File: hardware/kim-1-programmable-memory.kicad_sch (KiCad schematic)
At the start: 21 parts, among them J1 Conn_02x01, J3 EDGE_CONN, Q1 DMG2305UX, SW1 RESET, U1 74LVC541, U2 74LVC541, U3 74LVC245, U4 74LVC1G04, U6 74LVC1G38, U7 74LVC1G27, U8 PicoW

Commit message: New board design usign the RAMRW line
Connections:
- net RAMR~{W}: now reaches J3.Z (RAMRW)
- net RAMR~{W}: now also U4.2
- net R/~{W}: no longer names the net of J3.V (R/~{W})
- net R/~{W}: no longer U4.2
- net ~{R}/W: no longer names the net of J3.W (~{R}/W)
- net ~{R}/W: no longer U3.1 (A->B)
- net ~{R}/W' renamed RAM~{R}W
- net RAM~{R}W: now also U3.1 (A->B)
- no-connect marks 17 -> 18
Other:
- moved on the sheet: C1, C2, C3, C4, R2, SW1, U1, U2, U3, U4

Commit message: New board design
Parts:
- removed C4: 100nF, Capacitor_SMD:C_0603_1608Metric_Pad1.08x0.95mm_HandSolder, symbol Device:C_Small
- removed U4: 74LVC1G04, Package_TO_SOT_SMD:SOT-23-5_HandSoldering, symbol 74xGxx:74LVC1G04
- added C1, C11, C7: 100nF, Capacitor_SMD:C_0603_1608Metric_Pad1.08x0.95mm_HandSolder, symbol Device:C_Small
- added C10: 10uF, Capacitor_SMD:C_0603_1608Metric_Pad1.08x0.95mm_HandSolder, symbol Device:C_Small
- added D1: HDD, LED_SMD:LED_0603_1608Metric_Pad1.05x0.95mm_HandSolder, symbol Device:LED_Small
- added J3: VGA, Connector_Dsub:DSUB-15-HD_Female_Horizontal_P2.29x1.98mm_EdgePinOffset3.03mm_Housed_MountingHolesOffset4.94mm, symbol Connector:DA15_Receptacle_MountingHoles
- added J4: VIdeo Out, CUI_Devices:CUI_RCJ-014, symbol Connector:Conn_Coaxial_Small
- added J5: Micro_SD_Card_Det1, Micro-SD:SD_Card_Holder_SMD_WQ21801-B2180-7F, symbol Connector:Micro_SD_Card_Det1
- added R10, R11, R8, R9: 40R, Resistor_SMD:R_0603_1608Metric_Pad0.98x0.95mm_HandSolder, symbol Device:R_Small_US
- added R12: 470R, Resistor_SMD:R_0603_1608Metric_Pad0.98x0.95mm_HandSolder, symbol Device:R_Small_US
- added R13, R14, R15, R16: 270R, Resistor_SMD:R_0603_1608Metric_Pad0.98x0.95mm_HandSolder, symbol Device:R_Small_US
- added R17, R18: 47R, Resistor_SMD:R_0603_1608Metric_Pad0.98x0.95mm_HandSolder, symbol Device:R_Small_US
- added R19: 100R, Resistor_SMD:R_0603_1608Metric_Pad0.98x0.95mm_HandSolder, symbol Device:R_Small_US
- added R3: 5K1, Resistor_SMD:R_0603_1608Metric_Pad0.98x0.95mm_HandSolder, symbol Device:R_Small_US
- added R4, R7: 10K, Resistor_SMD:R_0603_1608Metric_Pad0.98x0.95mm_HandSolder, symbol Device:R_Small_US
- added U1, U7: LVC04, Package_SO:SOIC-14_3.9x8.7mm_P1.27mm, symbol 74xx:74HCT04
- C8: footprint Capacitor_SMD:C_0603_1608Metric_Pad1.08x0.95mm_HandSolder -> Capacitor_SMD:C_0805_2012Metric_Pad1.18x1.45mm_HandSolder
- R2: value 3K3 -> 5K1
- renumbered C6 to C2, C1 to C3, C2 to C4, C3 to C5, C7 to C6, J3 to J2, U6 to U2, U1 to U3, U2 to U4, U3 to U5, U7 to U6
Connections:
- net +3.3V: now also C1.2, C10.2, C11.2, C7.2, J5.4 (VDD), R3.2, R4.2, R7.2, U1.14 (VCC), U7.14 (VCC)
- net DB0: now also U5.18 (B0); no longer U5.9 (A7)
- net DB1: now also U5.17 (B1); no longer U5.8 (A6)
- net DB2: now also U5.16 (B2); no longer U5.7 (A5)
- net DB3: now also U5.15 (B3); no longer U5.6 (A4)
- net DB4: now also U5.14 (B4); no longer U5.5 (A3)
- net DB5: now also U5.13 (B5); no longer U5.4 (A2)
- net DB6: now also U5.12 (B6); no longer U5.3 (A1)
- net DB7: now also U5.11 (B7); no longer U5.2 (A0)
- net GND: now also C1.1, C10.1, C11.1, C7.1, J3.0 (PAD), J3.10 (P10), J3.5, J3.6, J3.7, J3.8, J4.2 (Ext), J5.10 (SHIELD), J5.6 (VSS), R19.1, U1.3, U1.7 (GND), U7.7 (GND); no longer U4.1 (G1)
- net ~{CE}: now also U8.26 (GPIO20), U1.1; no longer U8.21 (GPIO16)
- net ~{R}/W: now reaches J2.W (~{R}/W)
- net ~{R}/W: now also U1.13
- net ~{Ø2}: now reaches J2.Y (~{Ø2})
- net ~{Ø2}: now also U1.5
- net A0 renamed AD0
- net AD0: now also U5.2 (A0)
- net A1 renamed AD1
- net AD1: now also U5.3 (A1)
- net A2 renamed AD2
- net AD2: now also U5.4 (A2)
- net A3 renamed AD3
- net AD3: now also U5.5 (A3)
- net A4 renamed AD4
- net AD4: now also U5.6 (A4)
- net A5 renamed AD5
- net AD5: now also U5.7 (A5)
- net A6 renamed AD6
- net AD6: now also U5.8 (A6)
- net A7 renamed AD7
- net AD7: now also U5.9 (A7)
- net D0 renamed HSYNC
- net HSYNC: now also U7.11, U7.5; no longer U5.11 (B7)
- net D1 renamed VSYNC
- net VSYNC: now also U1.9; no longer U5.12 (B6)
- net D2 renamed Ø2
- net Ø2: now also U1.6; no longer U5.13 (B5)
- net D3 renamed R/~{W}
- net R/~{W}: now also U5.1 (A->B), U1.12; no longer U5.14 (B4)
- removed net D4: U5.15 (B3), U8.26 (GPIO20)
- net D5 renamed TX
- net TX: now also R9.1; no longer U5.16 (B2)
- net D6 renamed SCK
- net SCK: now also R10.1; no longer U5.17 (B1)
- net D7 renamed CSn
- net CSn: now also R8.1; no longer U5.18 (B0)
- net RAMR~{W}: no longer names the net of J2.Z (RAMRW)
- net RAM~{R}W renamed VIDEO
- net VIDEO: now also U7.1, U7.13, U7.3, U7.9; no longer U5.1 (A->B)
- new net: J4.1 (In), R12.1, R13.1
- new net: J5.3 (CMD), R9.2
- new net: J3.13 (P13), R17.1
- new net: R17.2, U7.10
- new net: J3.2, R15.1
- new net: R15.2, U7.2
- new net: J3.3, R16.1
- new net: R16.2, U7.12
- new net: D1.1 (K), R19.2
- new net: D1.2 (A), U1.10
- new net: R3.1, U1.2, U4.1 (G1)
- new net: J3.1, R14.1
- new net: J3.14 (P14), R18.1
- new net: J5.2 (DAT3/CD), R4.1, R8.2, U1.11
- new net: R12.2, U7.6
- new net: R18.2, U1.8
- new net: R14.2, U7.4
- new net: J5.7 (DAT0), R11.2
- new net: R13.2, U7.8
- new net: J5.5 (CLK), R10.2
- new net RX: R11.1, R7.1, U8.21 (GPIO16)
- no-connect marks 18 -> 26
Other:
- note added: "B"
- note added: "G"
- note added: "H"
- note added: "R"
- note added: "V"
- moved on the sheet: C2, C3, C4, C5, C8, C9, J1, J2, Q1, R1, R2, SW1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

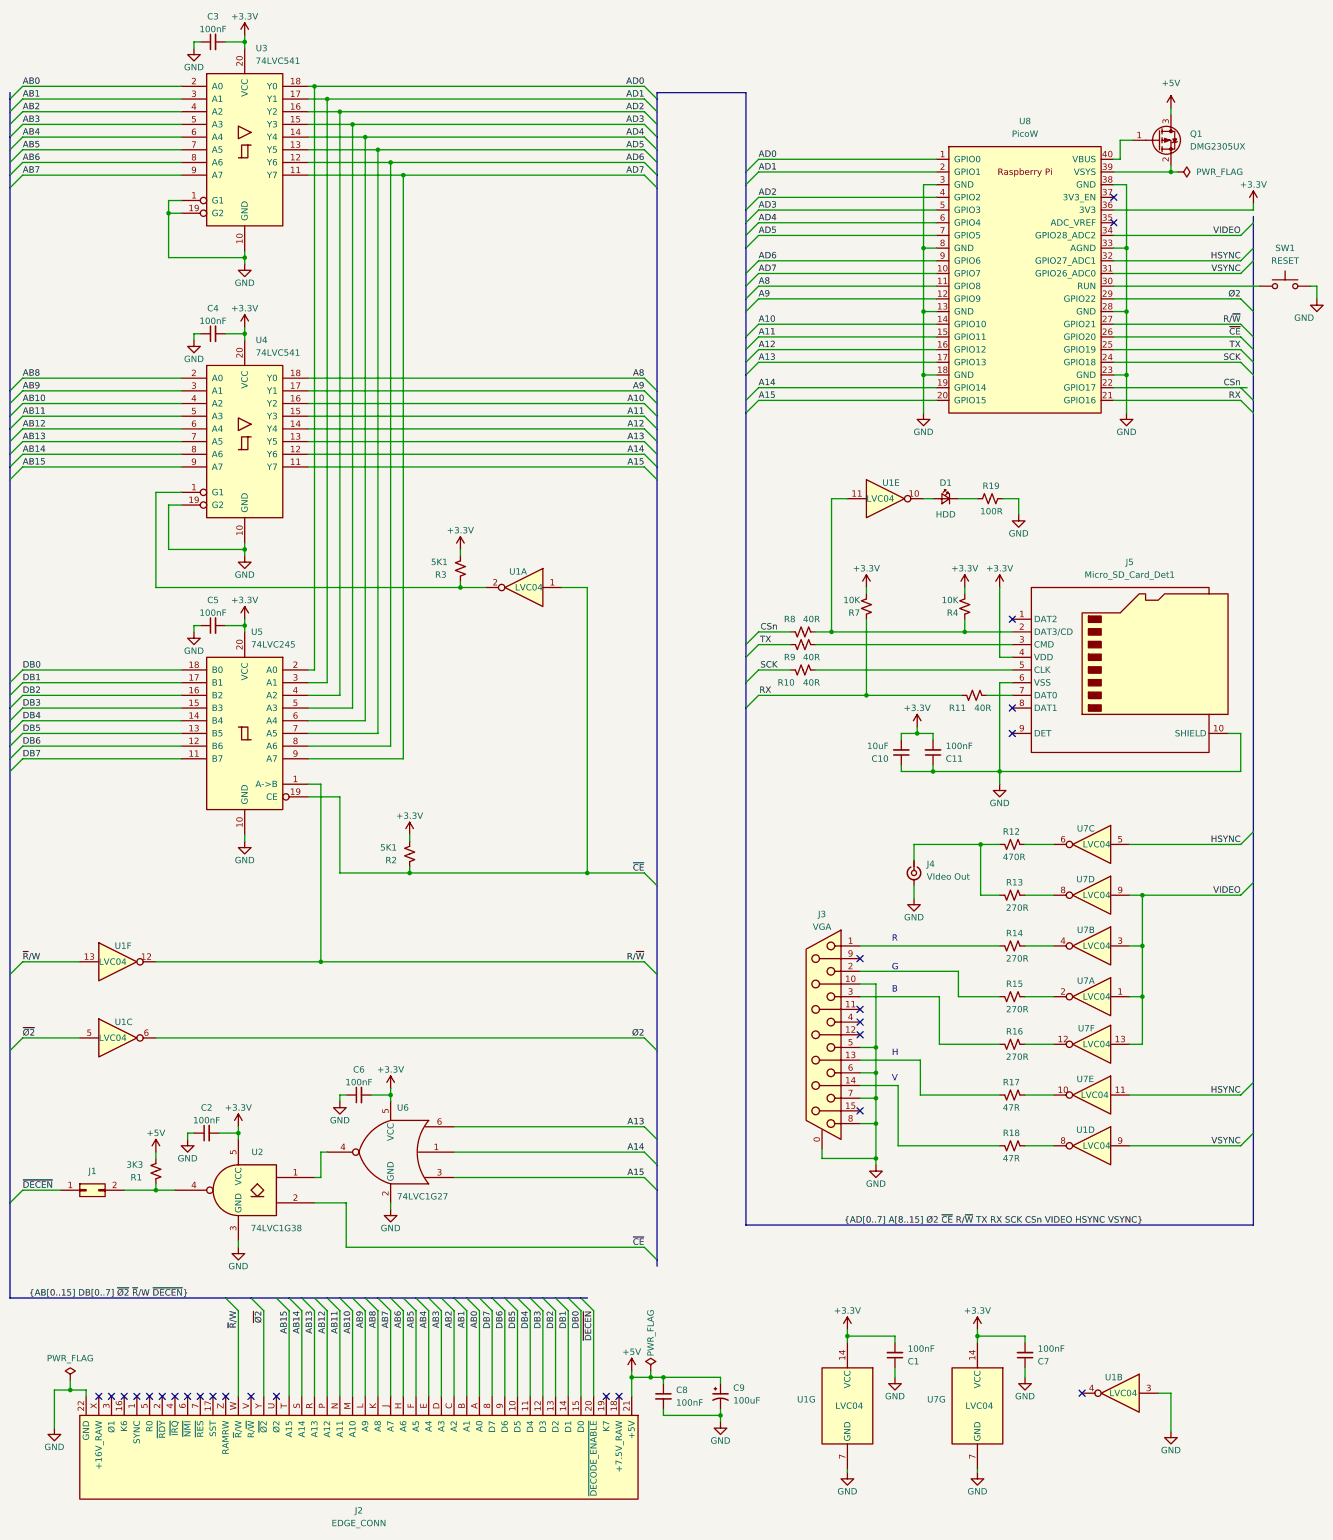
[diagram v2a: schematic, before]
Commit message: Add LCSC parts and correct video tracks impedance
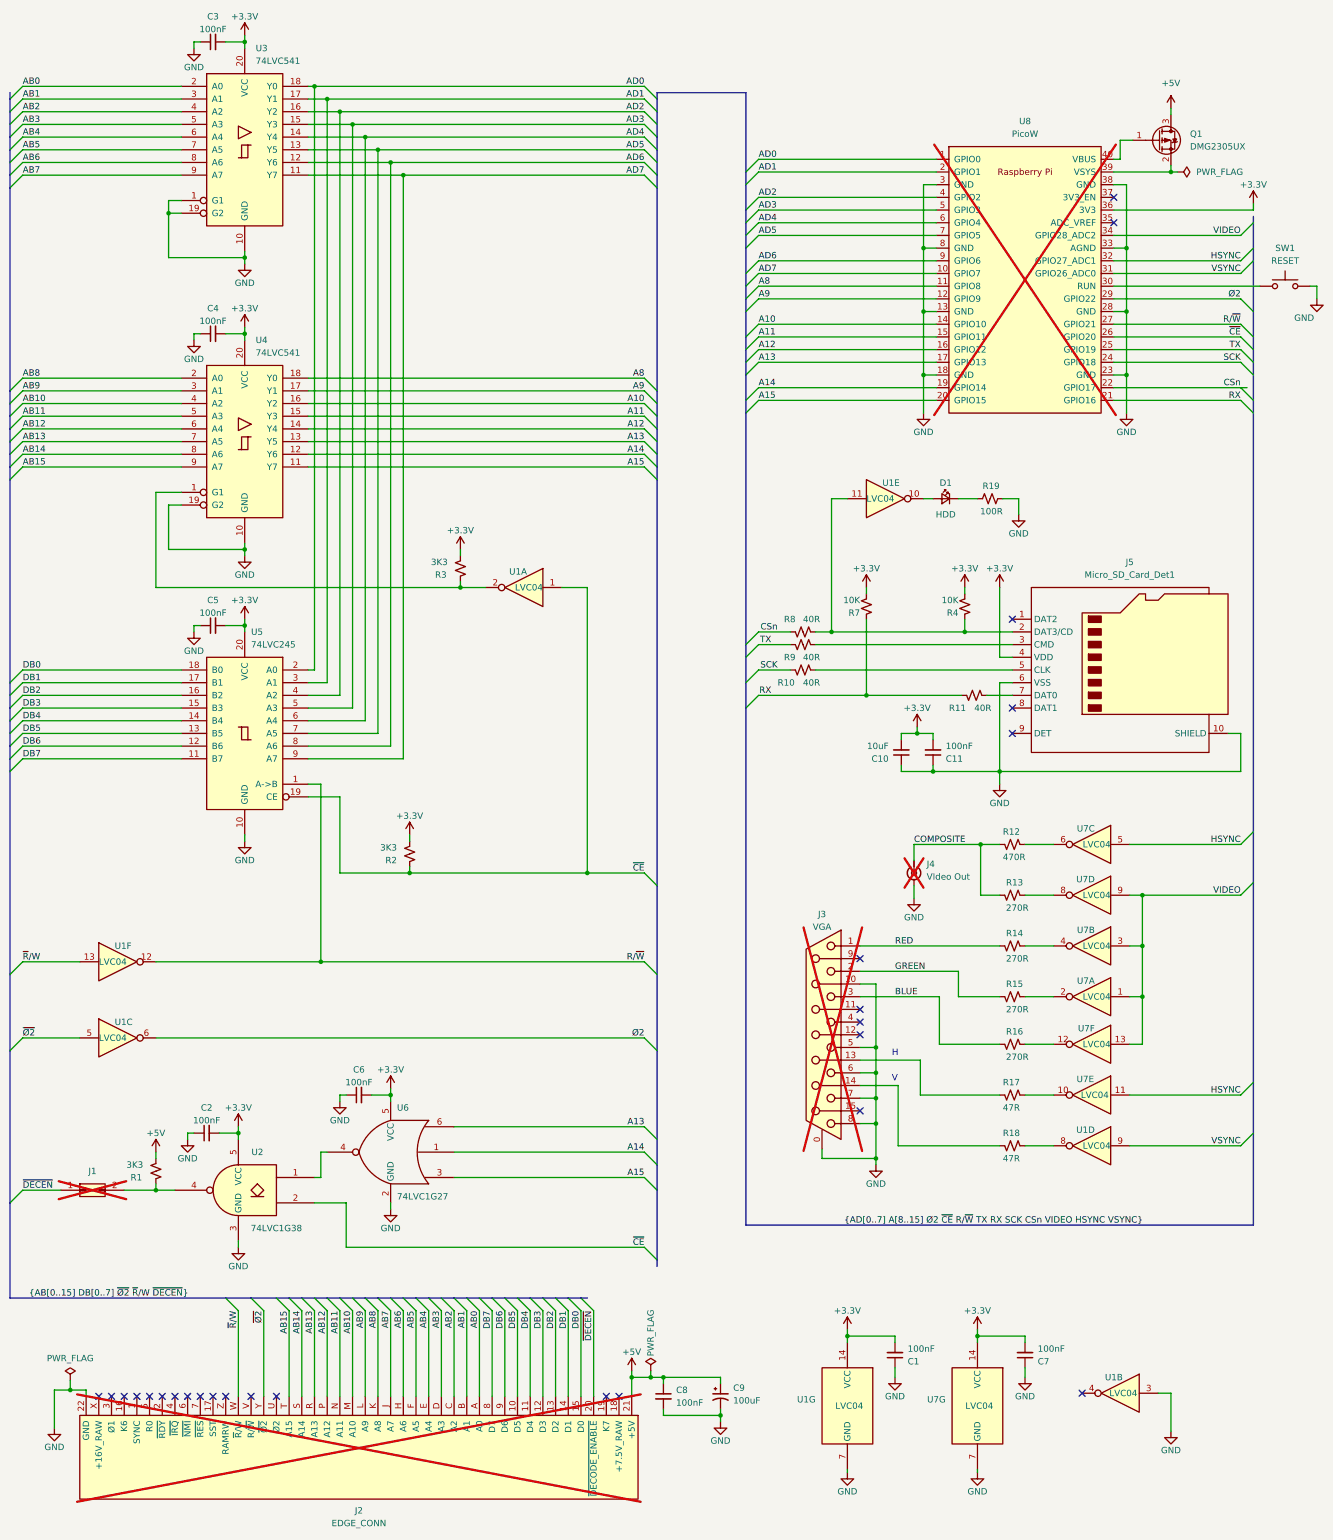
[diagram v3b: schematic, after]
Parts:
- C1, C11, C2, C3, C4, C5, C6, C7: LCSC (none) -> C77055
- C10: LCSC (none) -> C344022
- C8: LCSC (none) -> C77082
- C9: LCSC (none) -> C178540
- D1: LCSC (none) -> C497932
- J1, J2, J4, U8: now not fitted; now left out of the parts list
- J3: LCSC (none) -> C711364; now not fitted; now left out of the parts list
- J5: LCSC (none) -> C266620
- Q1: LCSC (none) -> C150470
- R1: LCSC (none) -> C25995
- R10, R11, R8, R9: LCSC (none) -> C23047
- R12: LCSC (none) -> C23179
- R13, R14, R15, R16: LCSC (none) -> C22966
- R17, R18: LCSC (none) -> C23182
- R19: LCSC (none) -> C159890
- R2, R3: value 5K1 -> 3K3; LCSC (none) -> C25995
- R4, R7: LCSC (none) -> C15401
- SW1: LCSC (none) -> C455245
- U1, U7: LCSC (none) -> C485074
- U2: LCSC (none) -> C2867613
- U3, U4: LCSC (none) -> C2652110
- U5: LCSC (none) -> C571201
- U6: LCSC (none) -> C128410
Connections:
- net COMPOSITE: now reaches J4.1 (In), R12.1, R13.1
- net GREEN: now reaches J3.2, R15.1
- net BLUE: now reaches J3.3, R16.1
- net RED: now reaches J3.1, R14.1
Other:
- note removed: "B"
- note removed: "G"
- note removed: "R"
